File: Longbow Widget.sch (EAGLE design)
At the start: 12 parts, among them X1 87832-14

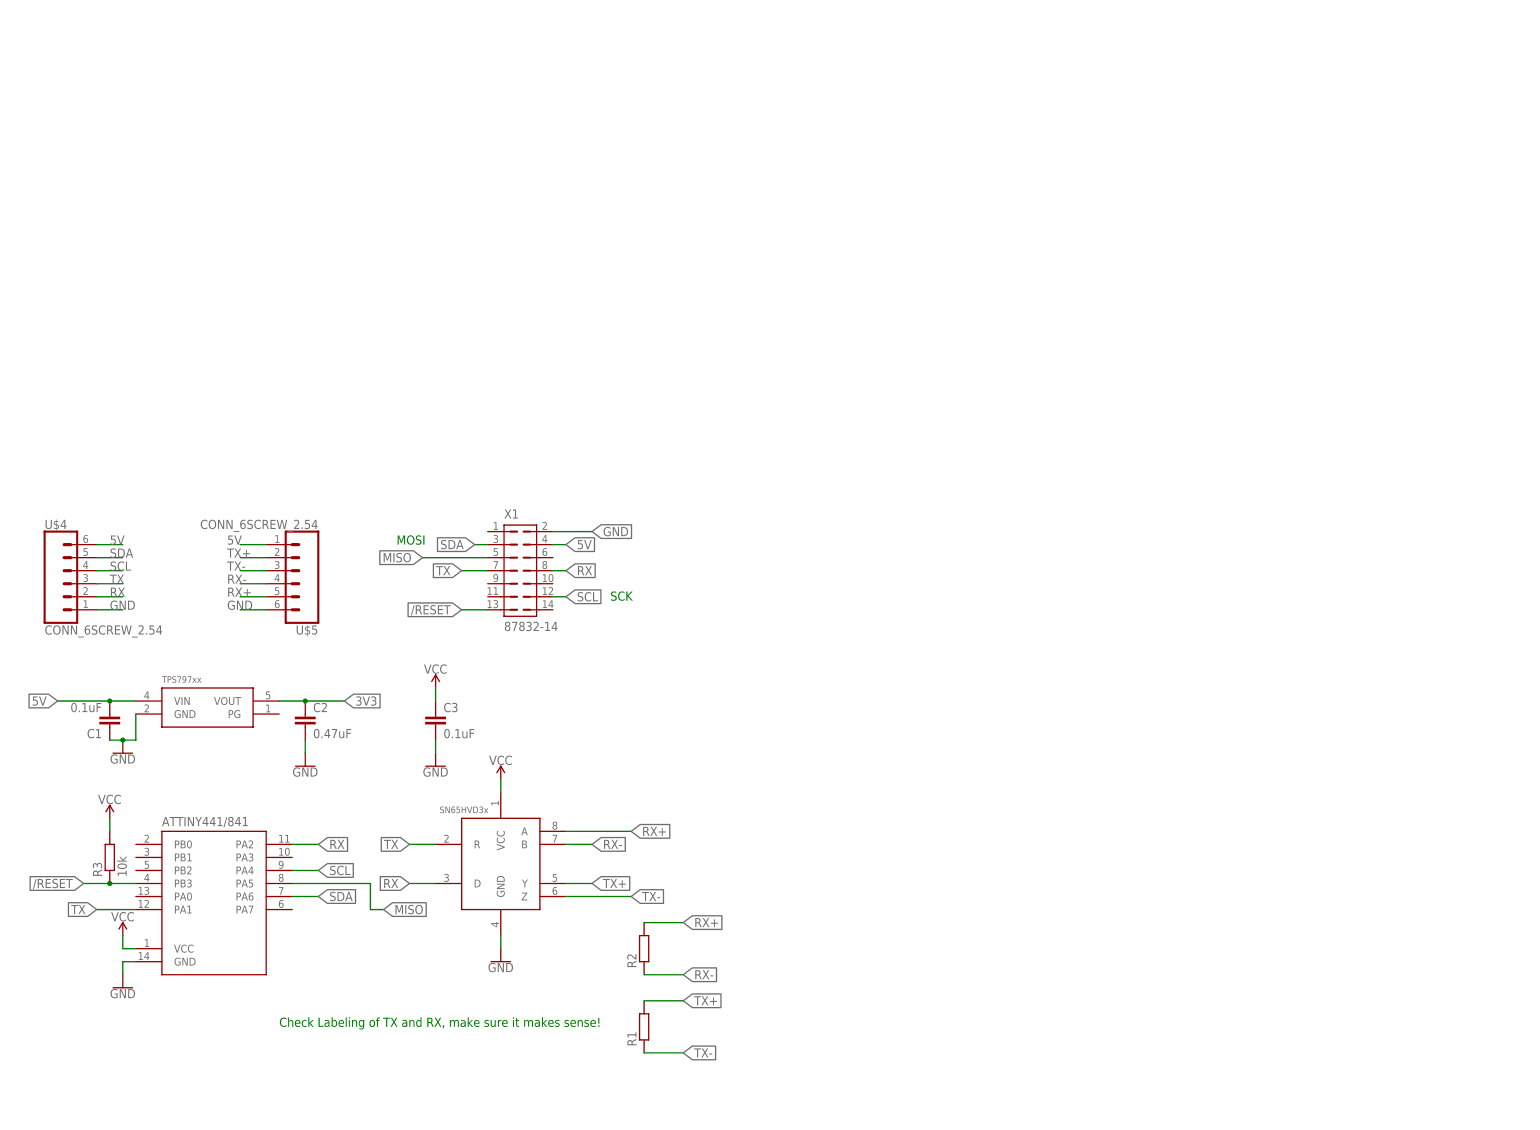
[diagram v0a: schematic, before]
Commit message: Updated Longbow Widget schematic, very preliminary board layout
Added fixes for many of the issues to the schematic, made very preliminary board layout

Likely to add some kind of transient protection to Longbow Widget, have left space on preliminary board layout to add in later
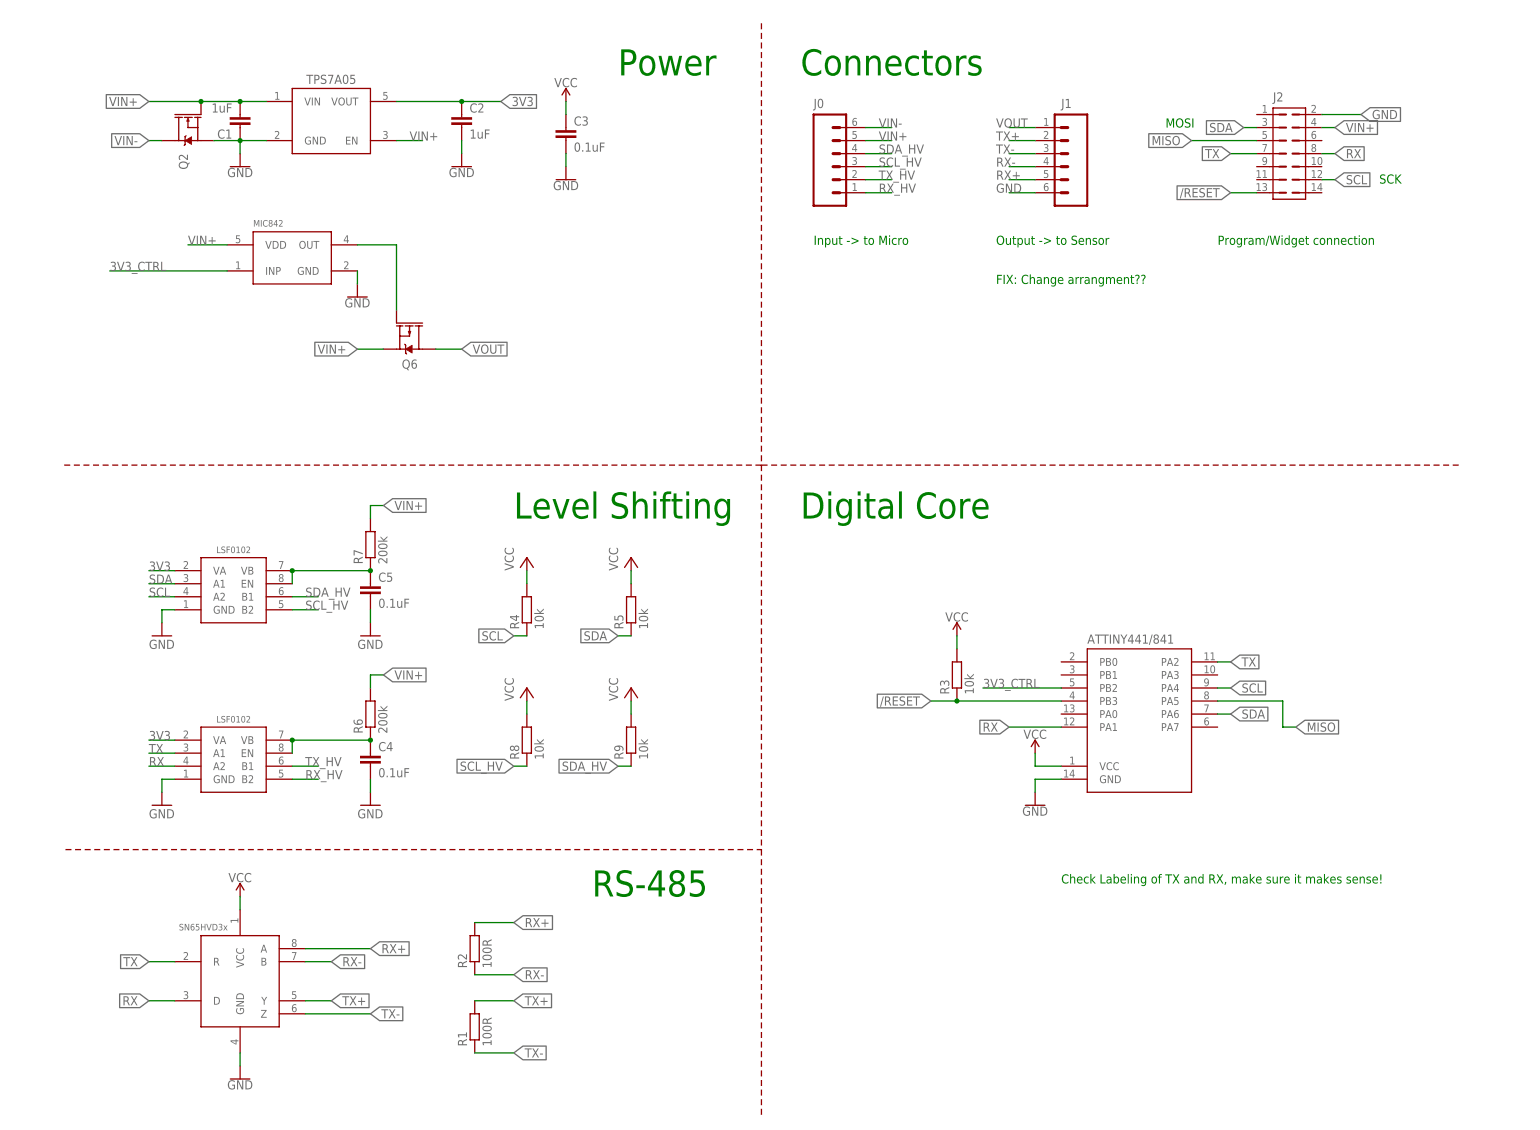
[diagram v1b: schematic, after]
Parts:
- removed U$4, U$5: CONN_6SCREW_2.54, bschulz:CONN_6SCREW_2.54
- removed X1: 87832-14, bschulz:87832-14
- added C4, C5: 0.1uF, bschulz_passives:C-EUC0603
- added J0, J1: CONN_6SCREW_2.54, bschulz:CONN_6SCREW_2.54
- added J2: 87832-14, bschulz:87832-14
- added Q2: DMG3404, bschulz:MOSFET-NCH-DMG3404L
- added Q6: FDN360P, bschulz:MOSFET_PCH-FDN360P
- added R4, R5, R8, R9: 10k, bschulz_passives:R-EU_10KR0402
- added R6, R7: 200k, bschulz_passives:R-EU_R0402
- added U$11: MIC842H, bschulz:MIC842H
- added U$6: LSF0102DQE, bschulz:LSF0102DQE
- added U1: TPS7A0533DBV, bschulz:TPS7A0533DBV
- C1: value 0.1uF -> 1uF; device bschulz_passives:C-EUC0603 -> bschulz_passives:C-EU1UFC0603
- C2: value 0.47uF -> 1uF; device bschulz_passives:C-EUC0603 -> bschulz_passives:C-EU1UFC0603
- R1, R2: value (none) -> 100R
- R3: device bschulz_passives:R-EU_R0603 -> bschulz_passives:R-EU_10KR0402
- U$3: value TPS79733 -> LSF0102DQE; device bschulz:TPS79733 -> bschulz:LSF0102DQE
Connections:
- removed net 5V: C1.2, U$3.VIN, U$4.6, U$5.1, X1.4
- new net 3V3_CTRL: U$11.INP, U$2.PB2
- new net GND1: Q2.S
- new net N$1: C5.1, R7.1, U$3.EN, U$3.VB
- new net N$3: C4.1, R6.1, U$6.EN, U$6.VB
- new net N$4: Q6.G, U$11.OUT
- new net RX_HV: J0.1, U$6.B2
- new net SCL_HV: J0.3, R8.1, U$3.B2
- new net SDA_HV: J0.4, R9.1, U$3.B1
- new net TX_HV: J0.2, U$6.B1
- new net VIN+: C1.2, J0.5, J2.4, Q2.G, Q6.S, R6.2, R7.2, R8.2, R9.2, U$11.VDD, U1.EN, U1.VIN
- new net VIN-: J0.6, Q2.D
- new net VOUT: J1.1, Q6.D
- net /RESET: now also J2.13; no longer X1.13
- net 3V3: now also R4.2, R5.2, U$3.VA, U$6.VA, U1.VOUT; no longer U$3.VOUT
- net GND: now also C4.2, C5.2, J1.6, J2.2, U$11.GND, U$6.GND, U1.GND; no longer U$4.1, U$5.6, X1.2
- net MISO: now also J2.5; no longer X1.5
- net RX: now also J2.8, U$2.PA1, U$6.A2; no longer U$2.PA2, U$4.2, X1.8
- net RX+: now also J1.5; no longer U$5.5
- net RX-: now also J1.4; no longer U$5.4
- net SCL: now also J2.12, R4.1, U$3.A2; no longer U$4.4, X1.12
- net SDA: now also J2.3, R5.1, U$3.A1; no longer U$4.5, X1.3
- net TX: now also J2.7, U$2.PA2, U$6.A1; no longer U$2.PA1, U$4.3, X1.7
- net TX+: now also J1.2; no longer U$5.2
- net TX-: now also J1.3; no longer U$5.3
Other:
- note added: "Connectors"
- note added: "Digital Core"
- note added: "FIX: Change arrangment??"
- note added: "Input -> to Micro"
- note added: "Level Shifting"
- note added: "Output -> to Sensor"
- note added: "Power"
- note added: "Program/Widget connection"
- note added: "RS-485"
- moved on the sheet: C1, C2, C3, R1, R2, R3

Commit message: Preliminary layout for Longbow Widget complete
Needs cleanup and changes to silk screen before review, should be nearly functional (should add polygon pours for power on input side). Also added preliminary BOM, which requires update with new parts and after adding additional part numbers (for pulse proof resistors, snub resistors, etc)
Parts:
- added D1, D2: (no value), bschulz:TVSSM712
- added R10, R11, R12, R13: 10R, bschulz_passives:R-EU_R0603
- C3, C4, C5: device bschulz_passives:C-EUC0603 -> bschulz_passives:C-EU0.1UFC0402
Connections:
- removed net GND1: Q2.S
- new net N$2: R10.1, U$1.A
- new net N$5: R11.1, U$1.B
- new net N$6: R12.1, U$1.Y
- new net N$7: R13.1, U$1.Z
- net GND: now also D1.COM, D2.COM, Q2.S
- net RX: now also J2.7, U$6.A1; no longer J2.8, U$6.A2
- net RX+: now also D1.D2, R10.2; no longer U$1.A
- net RX-: now also D1.D1, R11.2; no longer U$1.B
- net RX_HV: now also U$6.B1; no longer U$6.B2
- net TX: now also J2.8, U$6.A2; no longer J2.7, U$6.A1
- net TX+: now also D2.D1, R12.2; no longer U$1.Y
- net TX-: now also D2.D2, R13.2; no longer U$1.Z
- net TX_HV: now also U$6.B2; no longer U$6.B1
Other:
- moved on the sheet: R1, R2

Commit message: Cleaned up Widget
Cleaned up layout of widget, adjusted silkscreen, fixed pinout issue, generated final gerbers, ready for prototype
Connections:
- net GND: now also J1.1; no longer J1.6
- net RX+: now also J1.6; no longer J1.5
- net RX-: now also J1.5; no longer J1.4
- net TX+: now also J1.3; no longer J1.2
- net TX-: now also J1.4; no longer J1.3
- net VOUT: now also J1.2; no longer J1.1
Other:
- note removed: "FIX: Change arrangment??"
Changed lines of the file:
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@@
 <text x="185.42" y="170.18" size="1.778" layer="91">Output -&gt; to Sensor</text>
 <text x="228.6" y="170.18" size="1.778" layer="91">Program/Widget connection</text>
-<text x="185.42" y="162.56" size="1.778" layer="91">FIX: Change arrangment?? </text>
 </plain>
 <instances>
@@
 </segment>
 <segment>
-<pinref part="J1" gate="G$1" pin="6"/>
-<wire x1="193.04" y1="180.34" x2="187.96" y2="180.34" width="0.1524" layer="91"/>
-<label x="185.42" y="180.34" size="1.778" layer="95"/>
-</segment>
-<segment>
 <pinref part="J2" gate="G$1" pin="2"/>
 <wire x1="248.92" y1="195.58" x2="256.54" y2="195.58" width="0.1524" layer="91"/>
@@
 <pinref part="U1" gate="G$1" pin="GND"/>
 <wire x1="43.18" y1="190.5" x2="38.1" y2="190.5" width="0.1524" layer="91"/>
+</segment>
+<segment>
+<pinref part="J1" gate="G$1" pin="1"/>
+<wire x1="193.04" y1="193.04" x2="187.96" y2="193.04" width="0.1524" layer="91"/>
+<label x="185.42" y="193.04" size="1.778" layer="95"/>
 </segment>
 </net>
@@
 </net>
 <net name="TX+" class="0">
-<segment>
-<pinref part="J1" gate="G$1" pin="2"/>
-<wire x1="193.04" y1="190.5" x2="187.96" y2="190.5" width="0.1524" layer="91"/>
-<label x="185.42" y="190.5" size="1.778" layer="95"/>
-</segment>
 <segment>
 <pinref part="R12" gate="G$1" pin="2"/>
@@
 <wire x1="86.36" y1="17.78" x2="83.82" y2="17.78" width="0.1524" layer="91"/>
 </segment>
-</net>
-<net name="TX-" class="0">
 <segment>
 <pinref part="J1" gate="G$1" pin="3"/>
@@
 <label x="185.42" y="187.96" size="1.778" layer="95"/>
 </segment>
+</net>
+<net name="TX-" class="0">
 <segment>
 <wire x1="86.36" y1="12.7" x2="86.36" y2="5.08" width="0.1524" layer="91"/>
@@
 <wire x1="86.36" y1="12.7" x2="83.82" y2="12.7" width="0.1524" layer="91"/>
 </segment>
-</net>
-<net name="RX-" class="0">
 <segment>
 <pinref part="J1" gate="G$1" pin="4"/>
@@
 <label x="185.42" y="185.42" size="1.778" layer="95"/>
 </segment>
+</net>
+<net name="RX-" class="0">
 <segment>
 <label x="93.98" y="33.02" size="1.778" layer="95" xref="yes"/>
@@
 <junction x="91.44" y="33.02"/>
 </segment>
-</net>
-<net name="RX+" class="0">
 <segment>
 <pinref part="J1" gate="G$1" pin="5"/>
@@
 <label x="185.42" y="182.88" size="1.778" layer="95"/>
 </segment>
+</net>
+<net name="RX+" class="0">
 <segment>
 <label x="93.98" y="53.34" size="1.778" layer="95" xref="yes"/>
@@
 <junction x="91.44" y="53.34"/>
 </segment>
+<segment>
+<pinref part="J1" gate="G$1" pin="6"/>
+<wire x1="193.04" y1="180.34" x2="187.96" y2="180.34" width="0.1524" layer="91"/>
+<label x="185.42" y="180.34" size="1.778" layer="95"/>
+</segment>
 </net>
 <net name="MISO" class="0">
@@
 <net name="VOUT" class="0">
 <segment>
-<pinref part="J1" gate="G$1" pin="1"/>
-<wire x1="193.04" y1="193.04" x2="187.96" y2="193.04" width="0.1524" layer="91"/>
-<label x="185.42" y="193.04" size="1.778" layer="95"/>
-</segment>
-<segment>
 <pinref part="Q6" gate="G$1" pin="D"/>
 <wire x1="76.2" y1="149.86" x2="81.28" y2="149.86" width="0.1524" layer="91"/>
 <label x="81.28" y="149.86" size="1.778" layer="95" xref="yes"/>
 </segment>
-</net>
+<segment>
+<pinref part="J1" gate="G$1" pin="2"/>
+<wire x1="193.04" y1="190.5" x2="187.96" y2="190.5" width="0.1524" layer="91"/>
+<label x="185.42" y="190.5" size="1.778" layer="95"/>
+</segment>
+</net>
